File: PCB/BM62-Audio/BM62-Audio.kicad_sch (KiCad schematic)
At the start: 3 parts, among them J1 AudioJack3, J2 USB_C_Receptacle_USB2.0

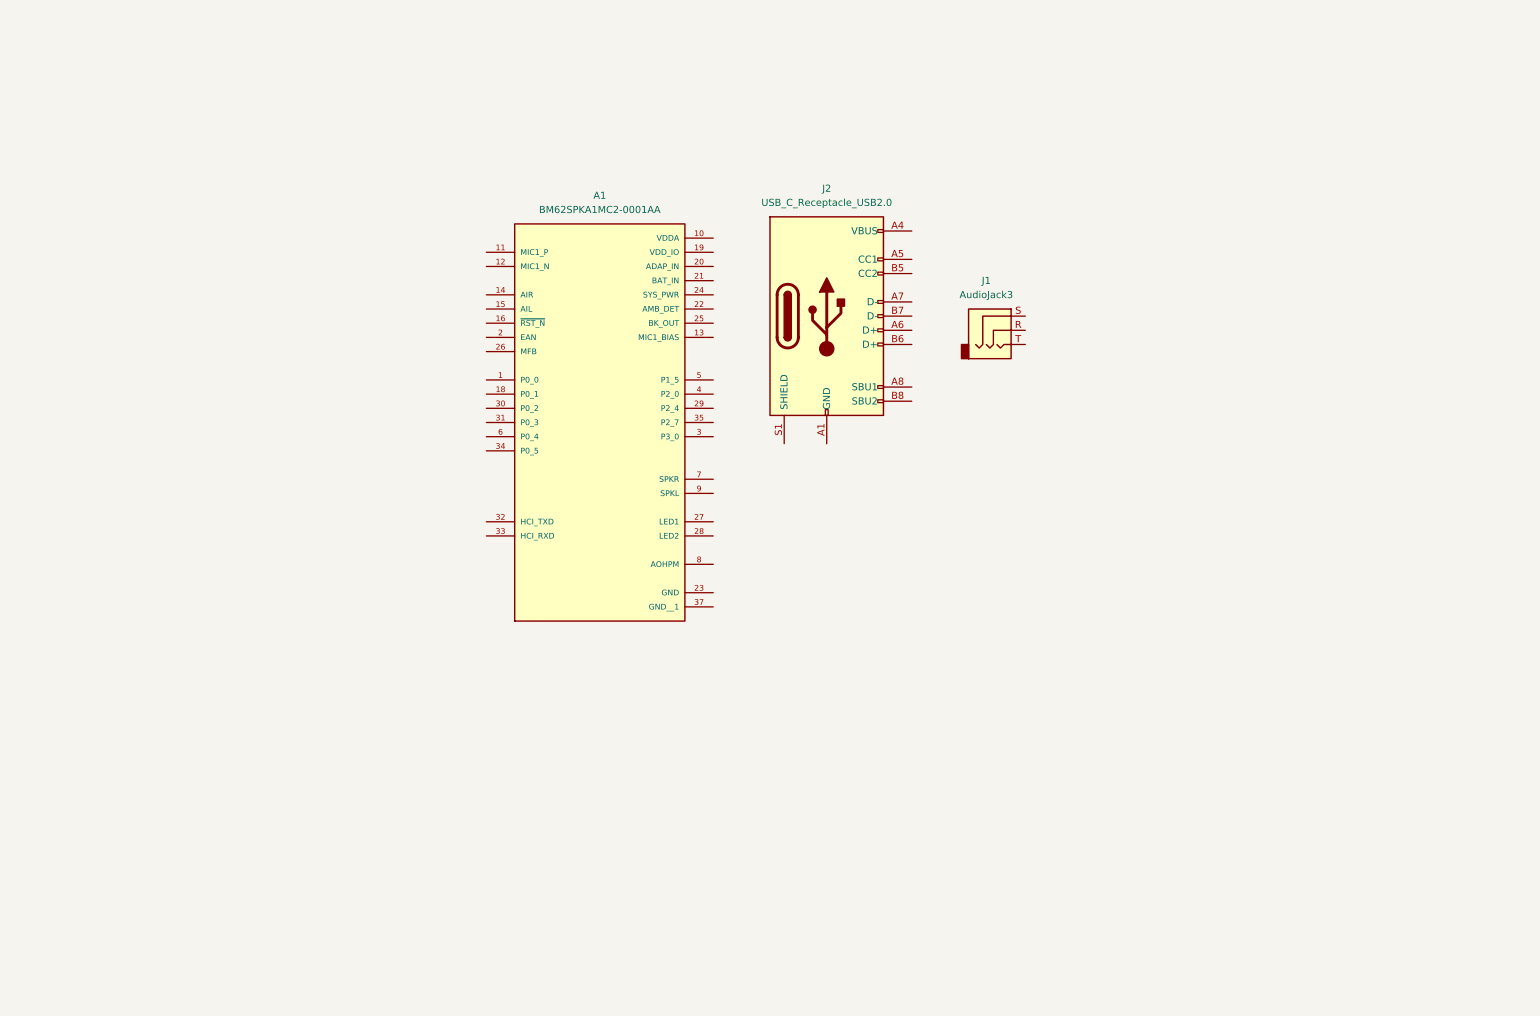
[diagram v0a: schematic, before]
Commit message: ✏️ 回路図の基礎ができた
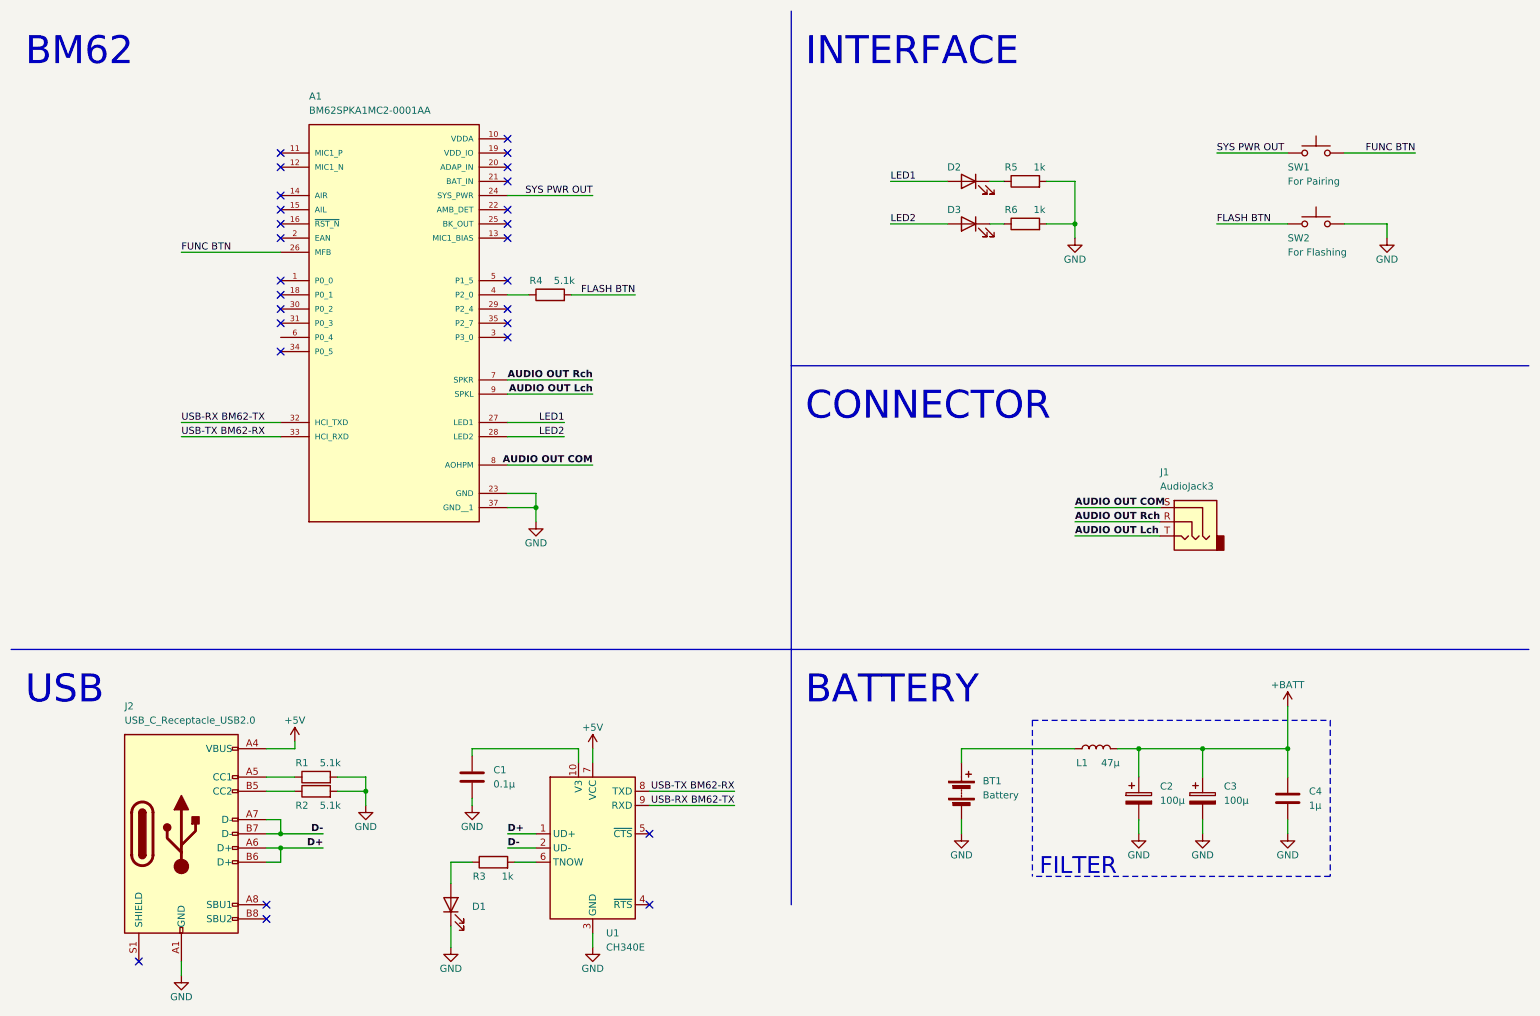
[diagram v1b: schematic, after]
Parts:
- added BT1: Battery, symbol Device:Battery
- added C1: 0.1µ, Capacitor_SMD:C_0603_1608Metric, symbol Device:C
- added C2, C3: 100µ, Capacitor_THT:CP_Radial_D6.3mm_P2.50mm, symbol Device:C_Polarized
- added C4: 1µ, Capacitor_SMD:C_0603_1608Metric, symbol Device:C
- added D1, D2, D3: WHITE, LED_SMD:LED_0603_1608Metric, symbol Device:LED
- added L1: 47µ, Inductor_SMD:L_6.3x6.3_H3, symbol Device:L
- added R1, R2, R4: 5.1k, Resistor_SMD:R_0603_1608Metric, symbol Device:R
- added R3, R5, R6: 1k, Resistor_SMD:R_0603_1608Metric, symbol Device:R
- added SW1: For Pairing, symbol Switch:SW_Push
- added SW2: For Flashing, symbol Switch:SW_Push
- added U1: CH340E, Package_SO:MSOP-10_3x3mm_P0.5mm, symbol Interface_USB:CH340E
- J2: footprint (none) -> Connector_USB:USB_C_Receptacle_Palconn_UTC16-G
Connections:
- net AUDIO OUT Rch: now reaches J1.R
- net AUDIO OUT Rch: now also A1.7 (SPKR)
- net AUDIO OUT COM: now reaches J1.S
- net AUDIO OUT COM: now also A1.8 (AOHPM)
- net AUDIO OUT Lch: now reaches J1.T
- net AUDIO OUT Lch: now also A1.9 (SPKL)
- net GND: now reaches A1.23 (GND)
- net GND: now also A1.37 (GND__1), J2.A1 (GND), J2.A12 (GND), J2.B1 (GND), J2.B12 (GND), BT1.2 (-), C1.2, C2.2, C3.2, C4.2, D1.1 (K), R1.2, R2.2, R5.2, R6.2, SW2.2, U1.3 (GND)
- net SYS PWR OUT: now reaches A1.24 (SYS_PWR)
- net SYS PWR OUT: now also SW1.1
- net FUNC BTN: now reaches A1.26 (MFB)
- net FUNC BTN: now also SW1.2
- net LED1: now reaches A1.27 (LED1)
- net LED1: now also D2.2 (A)
- net LED2: now reaches A1.28 (LED2)
- net LED2: now also D3.2 (A)
- net USB-RX BM62-TX: now reaches A1.32 (HCI_TXD)
- net USB-RX BM62-TX: now also U1.9 (RXD)
- net USB-TX BM62-RX: now reaches A1.33 (HCI_RXD)
- net USB-TX BM62-RX: now also U1.8 (TXD)
- net at A1.4 (P2_0): now also R4.1
- net +5V: now reaches J2.A4 (VBUS), J2.A9 (VBUS), J2.B4 (VBUS), J2.B9 (VBUS)
- net +5V: now also U1.7 (VCC)
- net at J2.A5 (CC1): now also R1.1
- net D+: now reaches J2.A6 (D+)
- net D+: now also J2.B6 (D+), U1.1 (UD+)
- net D-: now reaches J2.A7 (D-)
- net D-: now also J2.B7 (D-), U1.2 (UD-)
- net at J2.B5 (CC2): now also R2.1
- new net: D1.2 (A), R3.1
- new net: R3.2, U1.6 (TNOW)
- new net: C1.1, U1.10 (V3)
- new net: D3.1 (K), R6.1
- new net: BT1.1 (+), L1.1
- new net: D2.1 (K), R5.1
- new net +BATT: C2.1, C3.1, C4.1, L1.2
- new net FLASH BTN: R4.2, SW2.1
- no-connect marks 0 -> 27
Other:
- note added: "BATTERY"
- note added: "BM62"
- note added: "CONNECTOR"
- note added: "FILTER"
- note added: "INTERFACE"
- note added: "USB"
- moved on the sheet: A1, J1, J2
